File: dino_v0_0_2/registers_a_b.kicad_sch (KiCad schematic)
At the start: 21 parts, among them U31 74LS373, U32 74LS373, U33 74LS373, U35 74LS373, U41 74LS245, U42 74LS245, U43 74LS245, U44 74LS245, U5 74LS08, U57 74LS02, U66 74LS02

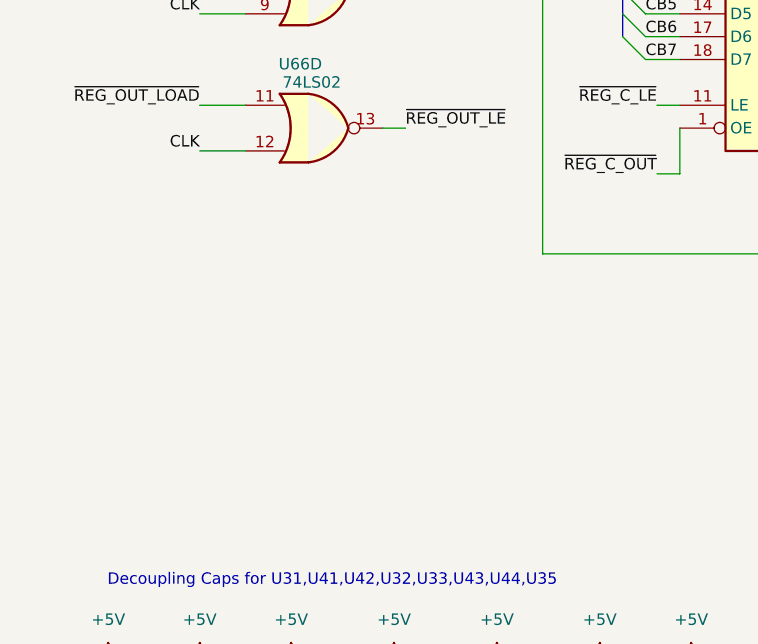
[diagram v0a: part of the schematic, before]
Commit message: feat(dino): complete v0.0.3 schematic — all 11 sheets netlist-clean
- wire MAR sheet: '373 LO/HI latches, 2x '245 M-bus drive, A15 decode
  (ROM_EN/~RAM_EN), LE stamps off /MAR_LO_LOAD//MAR_HI_LOAD
- fix PC_MAR_MUX polarity: PC '245s enabled on bit14=0, inverted vs
  bit-map convention (PC=1); add ~PC_MAR_MUX inverter, relabel U13/U14
- wire all 7 control-word bus taps [15:9] (SA0-2, END, PC_UP,
  PC_MAR_MUX, HALT) — label pairs had no wire between them
- untie NONE/NC '138 outputs: totem-pole bus fight on every microword;
  each unused output now individually no_connect
- build END (U61 NOR: ~MR = RESET|END, sync T-state clear) and HALT
  (T-state freeze via CET, clock keeps running)
- build COND/JNZ (U62: ~PC_LOAD = taken-JNZ | unconditional-JMP)
- claim src code 111 as /SW_OUT: IN port — DIP switches through 10k
  pull-ups onto W bus via '244; LED bank active-high off OB0-7
- add U66 missing power unit + decouplers (C63-C66)
- tools: kicad_gen_sheet.py (declarative YAML/JSON sheet generator,
  deterministic uuid5, collision-checked), kicad_xsheet_audit.py
  (cross-sheet contract audit); archive stale testing-strategy doc
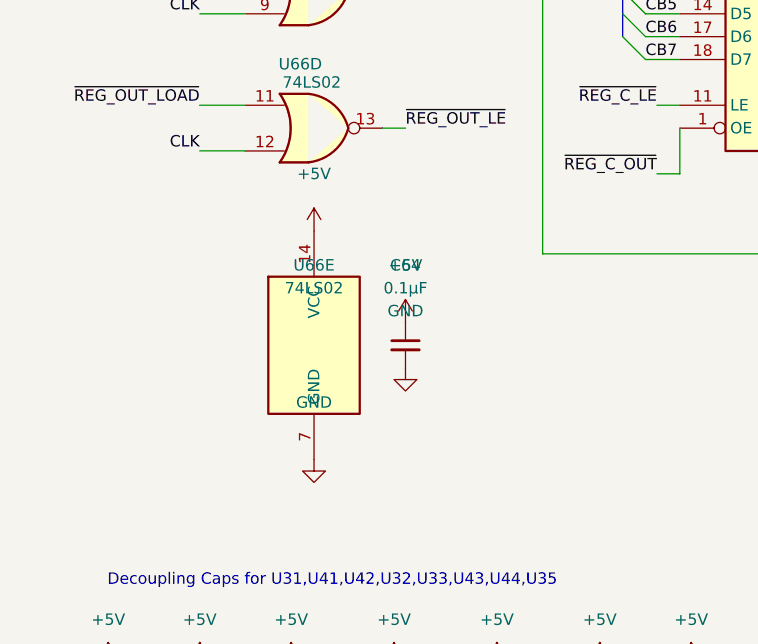
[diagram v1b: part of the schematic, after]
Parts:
- added C64: 0.1µF, symbol Device:C_Small
- added unit 5 of U66
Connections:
- net +5V: now also C64.1, U66.14 (VCC)
- net GND: now also C64.2, U66.7 (GND)

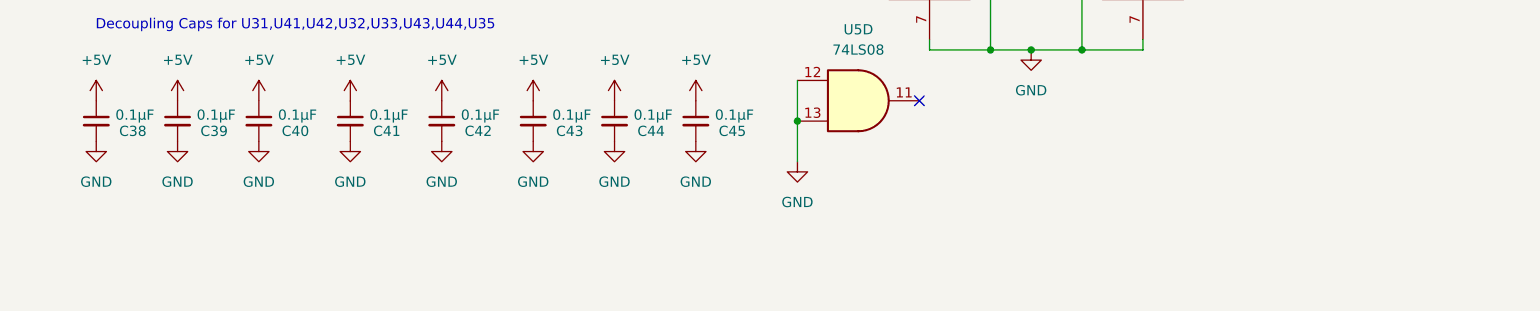
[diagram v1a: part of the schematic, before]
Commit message: feat(dino): generate + stamp per-sheet I/O contracts
Each module's boundary signals (IN/OUT/BIDIR with counterpart sheets)
derived from the kicad-cli netlist and placed as a text block on the
physical sheet, so a bench rig knows exactly what to drive and observe
per board. kicad_contracts.py regenerates both the markdown and the
stamps idempotently; stamping verified electrically neutral.
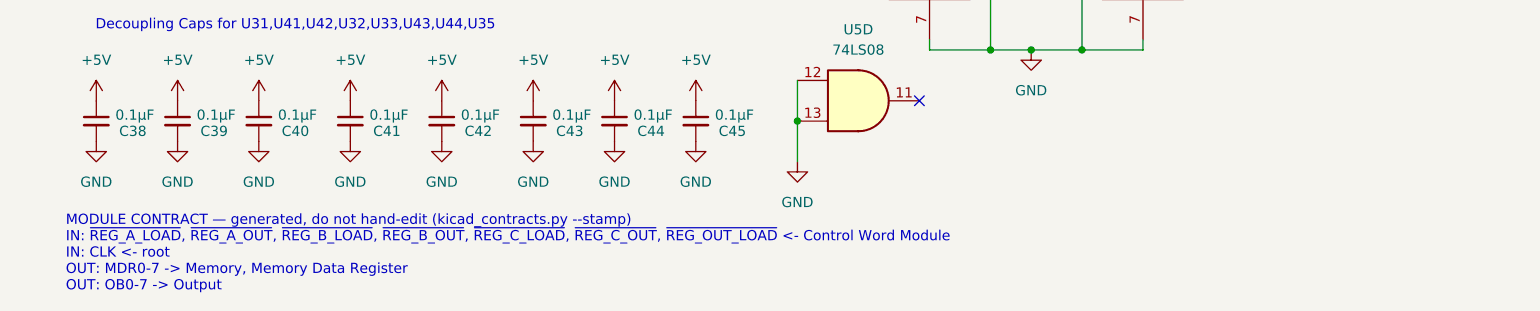
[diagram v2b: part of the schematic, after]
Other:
- note added: "MODULE CONTRACT — generated, do not hand-edit (kicad_contracts.py --stamp) IN: ~{REG_A_LOAD}, ~{REG_A_OUT}, ~{REG_B_LOAD}, ~{REG_B_OUT}, ~{REG_C_LOAD}, ~{REG_C_OUT}, ~{REG_OUT_LOAD} <- Control Word Module IN: CLK <- root OUT: MDR0-7 -> Memory, Memory Data Register OUT: OB0-7 -> Output"
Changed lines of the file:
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@@
+		)
+	)
+	(text "MODULE CONTRACT — generated, do not hand-edit (kicad_contracts.py --stamp)\nIN: ~{REG_A_LOAD}, ~{REG_A_OUT}, ~{REG_B_LOAD}, ~{REG_B_OUT}, ~{REG_C_LOAD}, ~{REG_C_OUT}, ~{REG_OUT_LOAD} <- Control Word Module\nIN: CLK <- root\nOUT: MDR0-7 -> Memory, Memory Data Register\nOUT: OB0-7 -> Output"
+		(exclude_from_sim no)
+		(at 15.24 211.93 0)
+		(effects
+			(font
+				(size 1.27 1.27)
+			)
+			(justify left bottom)
 		)
 	)

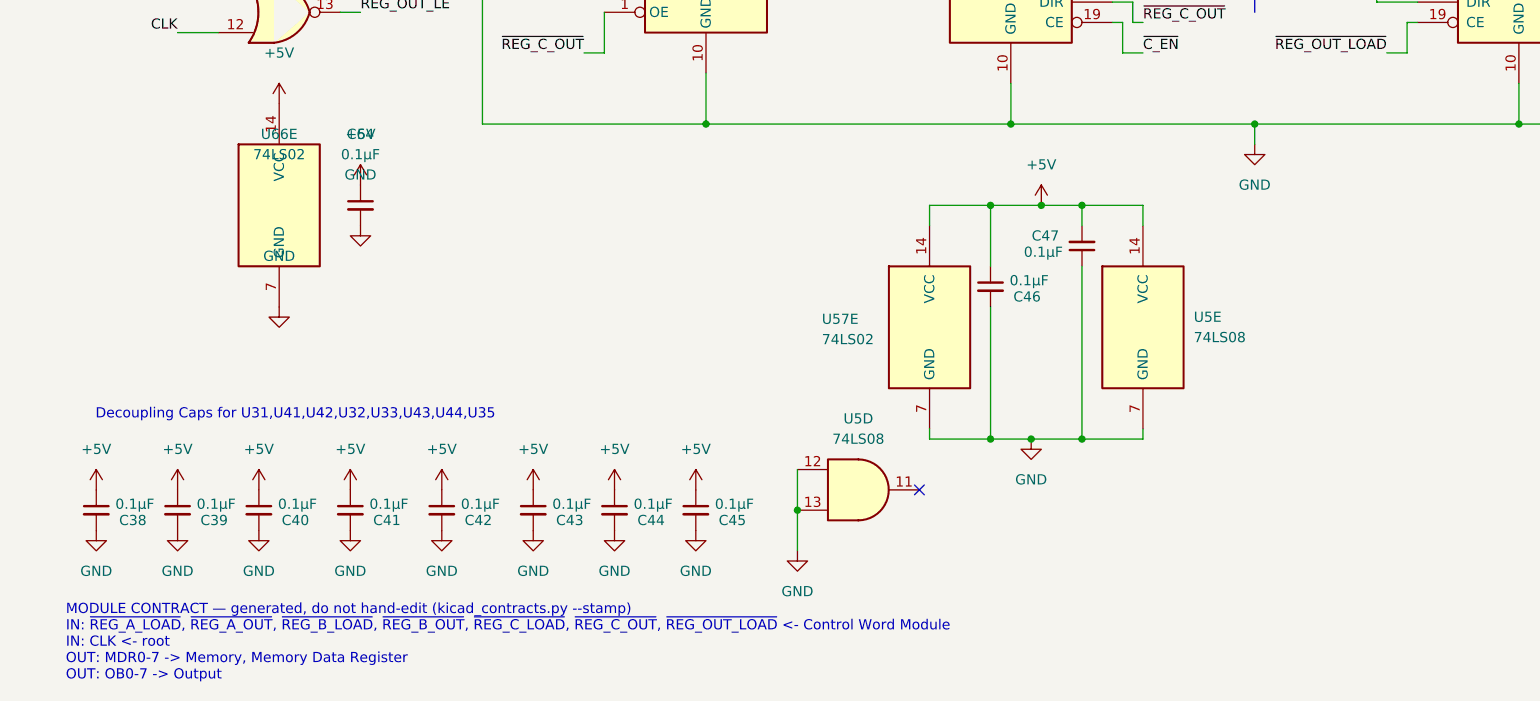
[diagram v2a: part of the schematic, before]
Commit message: fix(dino): three review-found schematic bugs on microcode/memory
- microcode U9/U15: ~WE tied +5V, A12 tied GND (were floating with NC
  flags — in-circuit corruption + image-aliasing hazard on AT28C64B)
- memory: label the U24.~OE/U19.CE net ~{ROM_OUT} — the ROM read path
  had no driver as drawn (caught by new kicad_netlist.py --lint)
- memory: U21 (RAM-side '245) CE now AND(~RAM_OUT, ~WRITE_DIR) via U51
  spare gates — was enabled by ~RAM_EN alone, buffering floating RAM DQ
  onto MDR against register drivers whenever MAR parked on a RAM
  address with no RAM op in flight

Contracts restamped; all verified in kicad_netlist.py + kicad-cli
export; lint clean project-wide.
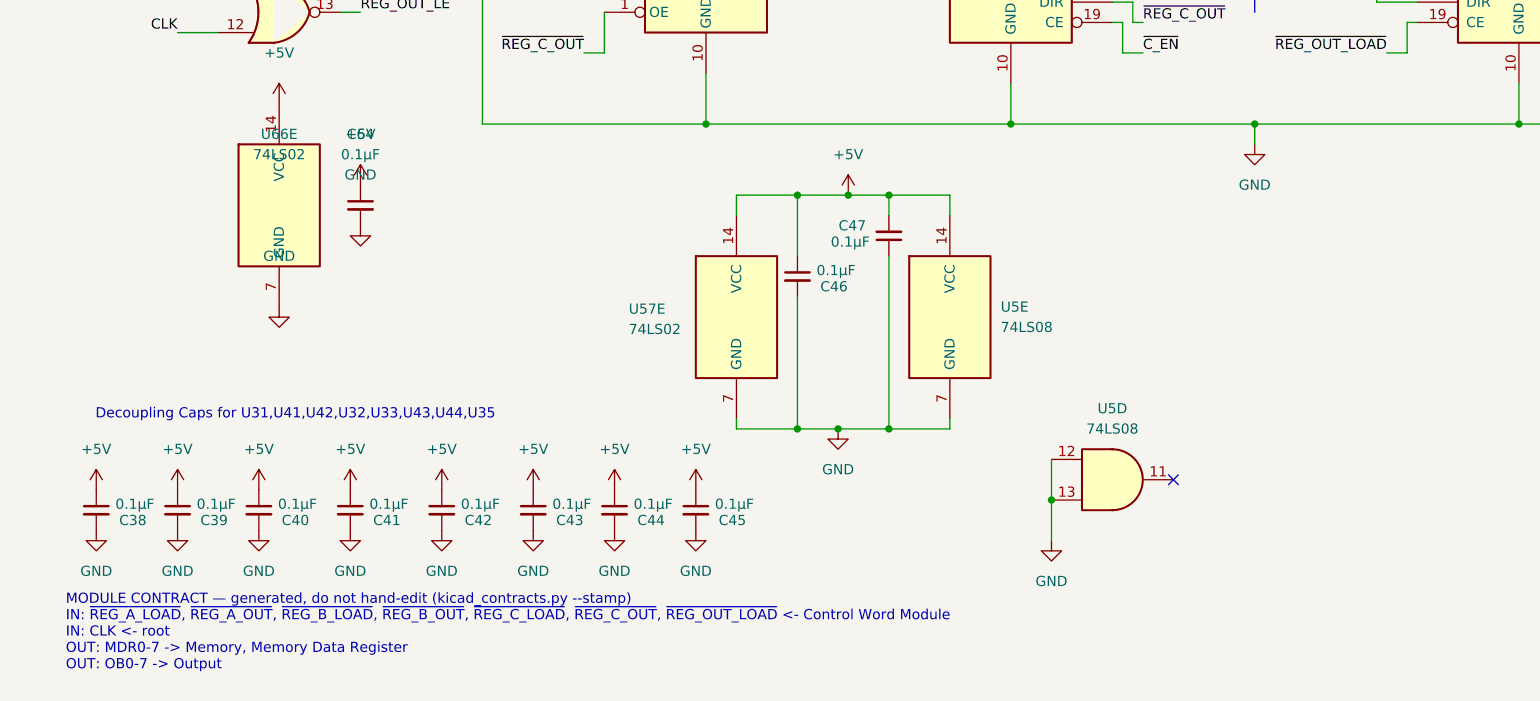
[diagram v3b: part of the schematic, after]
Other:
- moved on the sheet: C46, C47, U57E, U5D, U5E
